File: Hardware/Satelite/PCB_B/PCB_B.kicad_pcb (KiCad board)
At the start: 2 copper layers, 65 parts, among them IC1 MCP1642B-50I_MS, IC2 MCP1642B-50I_MS, J1 Conector_PCB_B-C, J2 Conector_PCB_A-B, U1 MIC5323-3.3YD5_TR, U2 ADP2108AUJ-3.3, U3 INA194, U4 MCP6001-OT, U5 INA194, U6 MCP6001-OT, U7 INA194, U8 BQ24091DGQT, U9 BQ27441DRZR-G1A

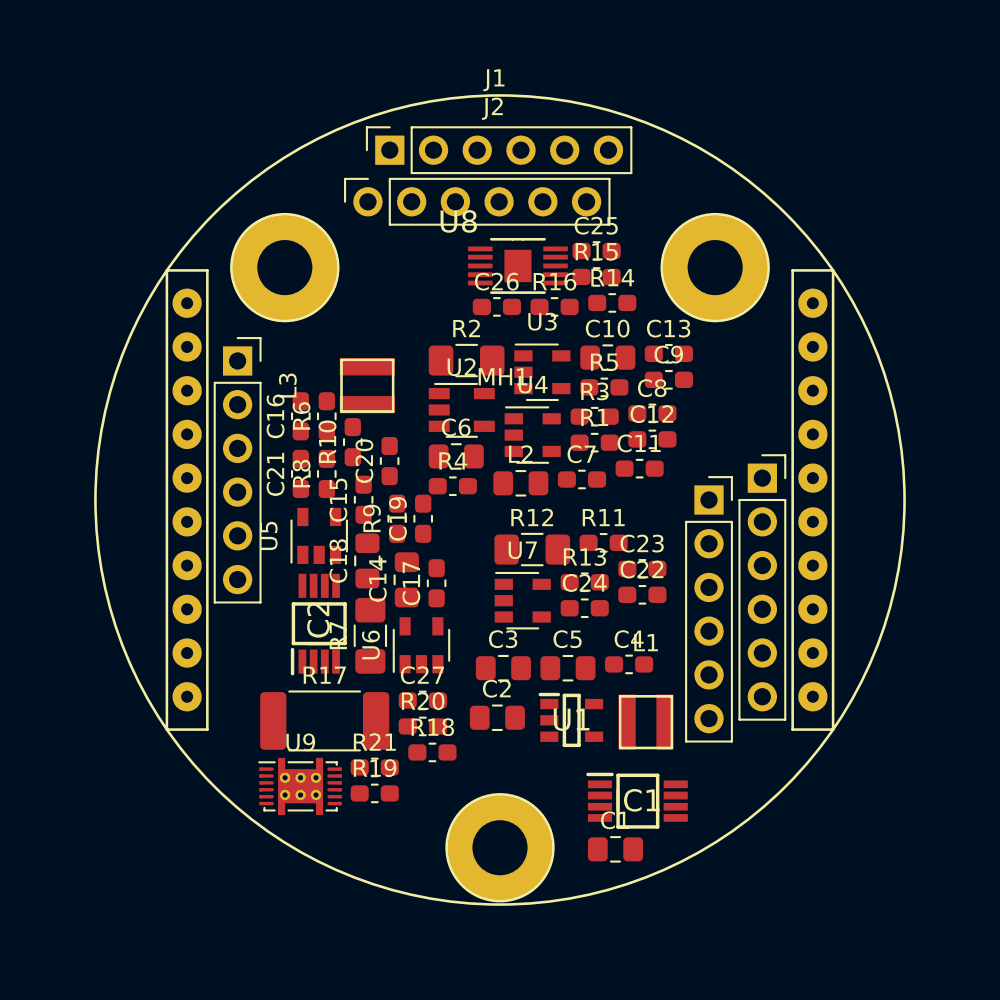
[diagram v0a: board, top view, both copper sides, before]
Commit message: Posicionamiento de conectores en PCB B
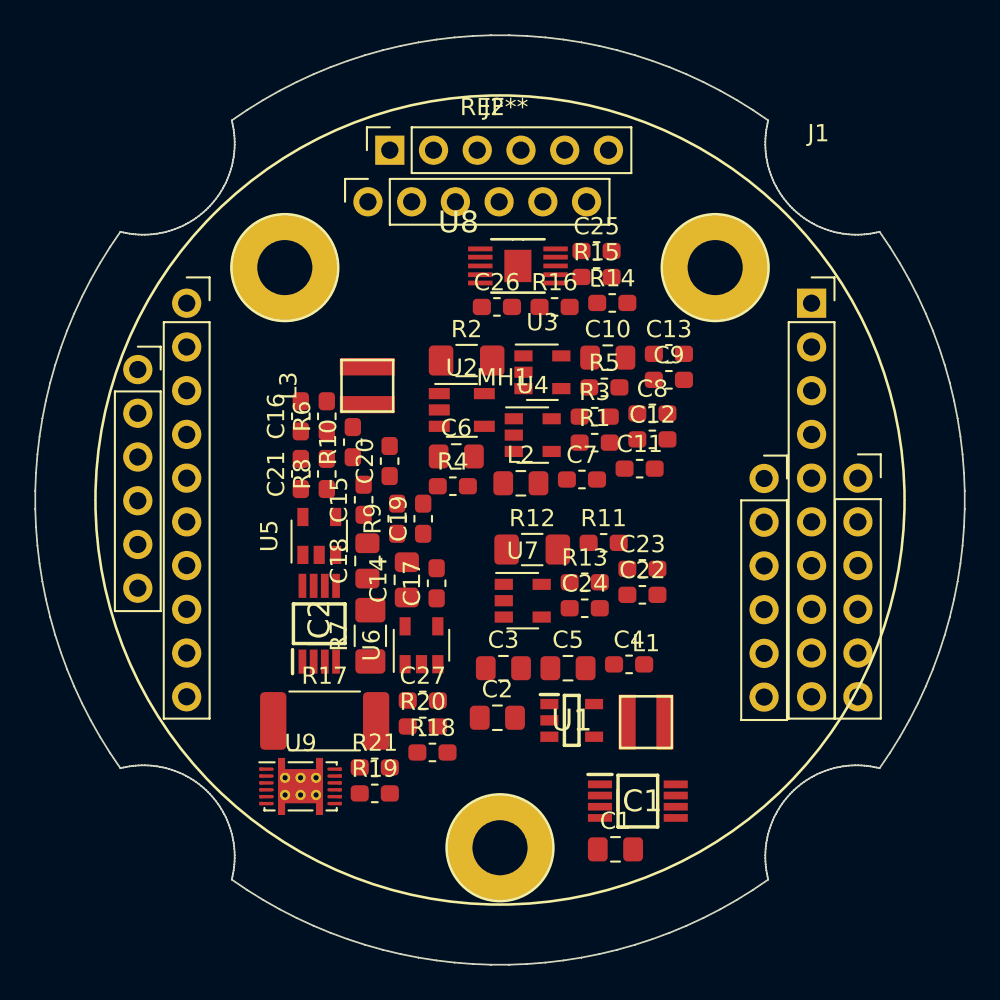
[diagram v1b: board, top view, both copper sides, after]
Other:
- board outline added: 54 x 54 mm

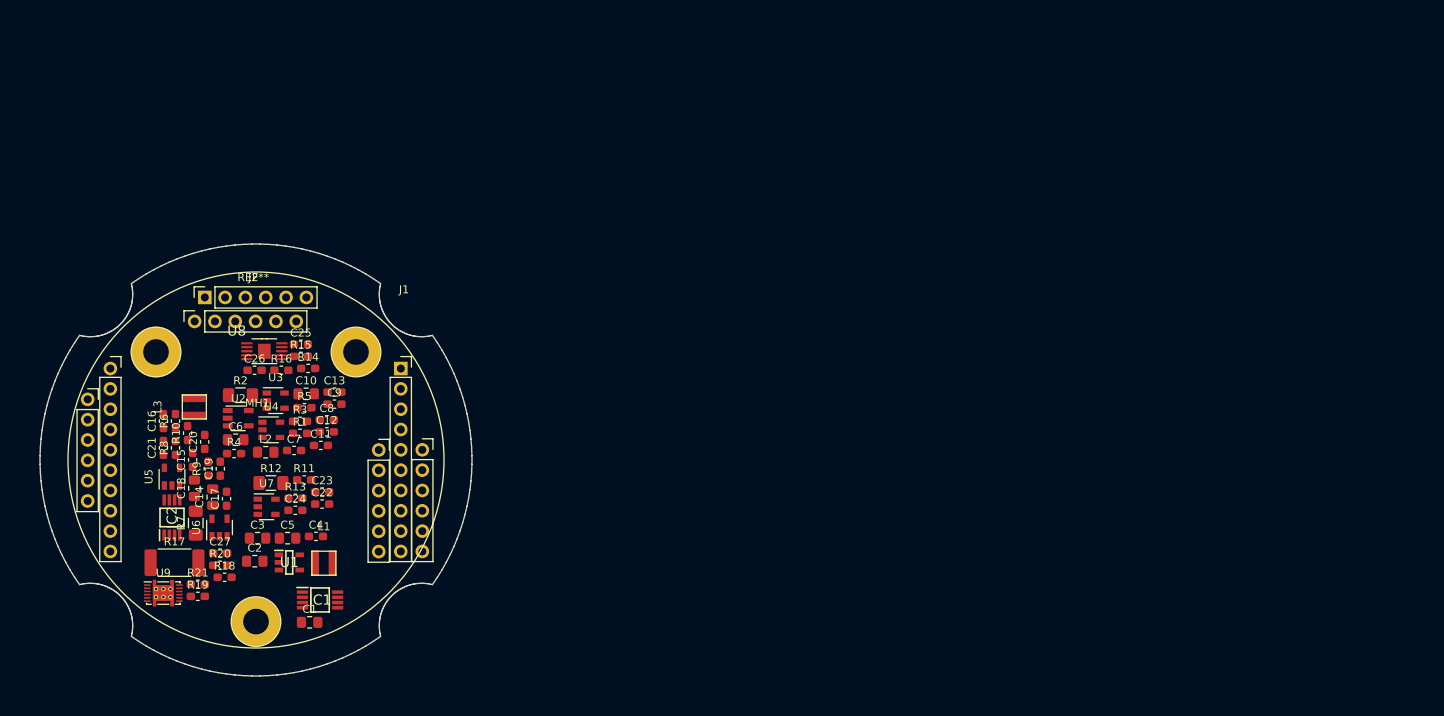
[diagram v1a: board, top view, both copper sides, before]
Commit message: Modificaciones en conectores, netlist para PCB C
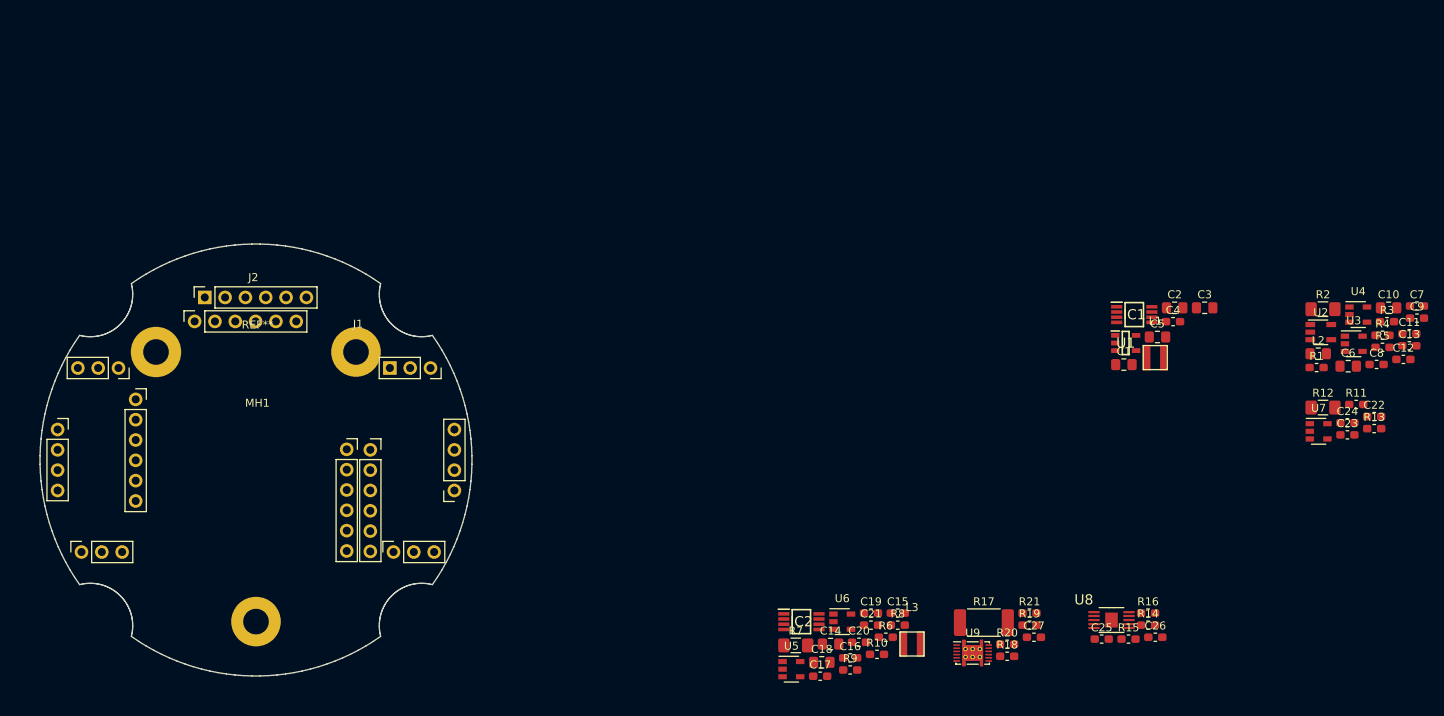
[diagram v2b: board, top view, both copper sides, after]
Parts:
- added REF**: PCB_mayor_diametro, AXTEC:PCB_mayor_diametro, F.Cu at (0.00, 0.00)
- moved R4 144.3 mm to (140.8, -15.6)
- moved C7 141.5 mm to (145.1, -19.2)
- moved C6 139.4 mm to (136.5, -11.7)
- moved C11 136.8 mm to (144.2, -15.8)
- moved U4 136.6 mm to (137.8, -18.2)
- moved R3 136.4 mm to (141.4, -17.3)
- moved C9 135.7 mm to (145.1, -17.7)
- moved R2 135.7 mm to (133.4, -18.9)
- moved U2 135.7 mm to (133.1, -16.0)
- moved C10 135.7 mm to (141.6, -19.0)
- moved R13 135.1 mm to (139.8, -3.92)
- moved R5 135.0 mm to (140.8, -14.1)
- moved U3 134.9 mm to (137.2, -14.5)
- moved C12 134.9 mm to (143.4, -12.6)
- moved C13 134.5 mm to (144.2, -14.3)
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
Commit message: Nuevo conector B-C
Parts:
- IC1, IC2: footprint SOP65P490X110-8N -> SamacSys_Parts:SOP65P490X110-8N
- U1: footprint SOT95P280X100-5N -> SamacSys_Parts:SOT95P280X100-5N

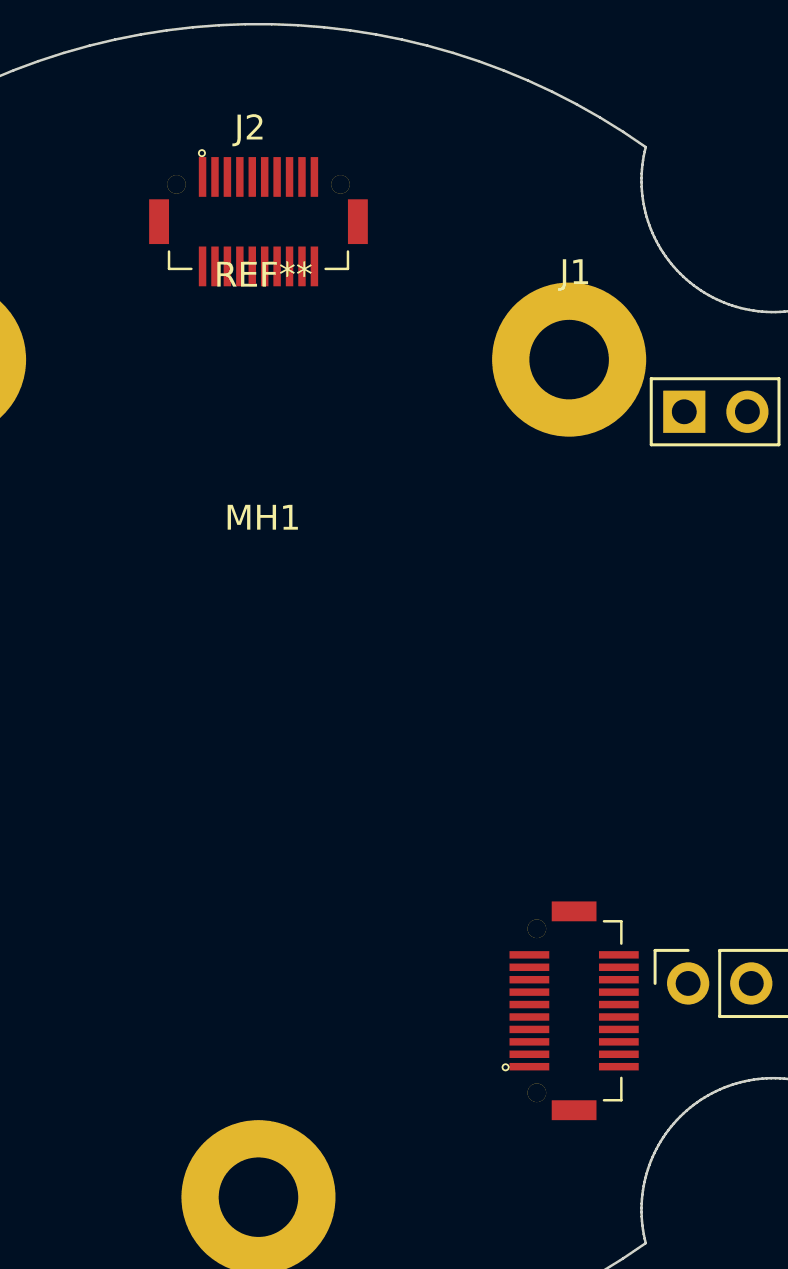
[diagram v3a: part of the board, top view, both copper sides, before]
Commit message: La parte del conector B-C que va en el PCB_B fue movido a bottom mientras que la parte que va en el PCB_C permanece en top
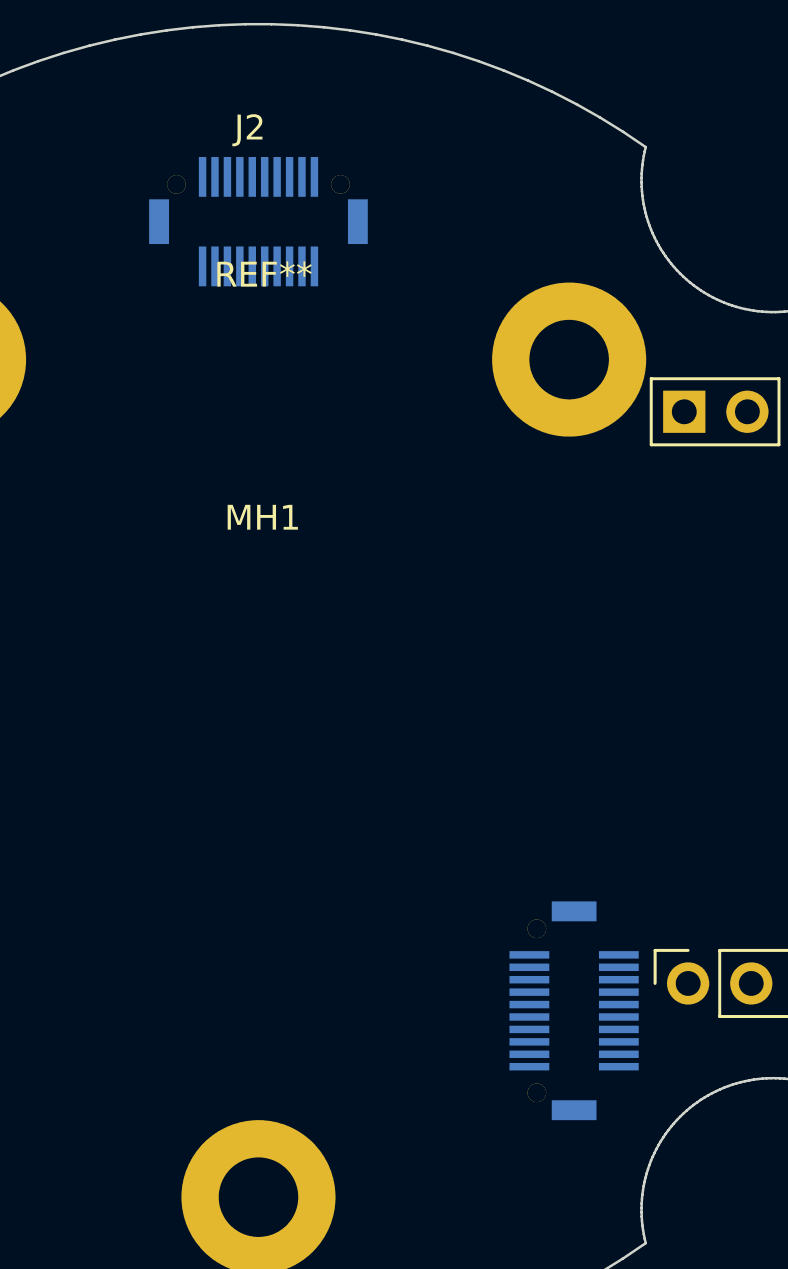
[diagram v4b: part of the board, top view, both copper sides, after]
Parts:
- IC1, IC2: footprint SamacSys_Parts:SOP65P490X110-8N -> SOP65P490X110-8N
- J1: footprint AXTEC:Conector_PCB_B-C -> AXTEC:Conector_PCB_B-C_Lado_B
- U1: footprint SamacSys_Parts:SOT95P280X100-5N -> SOT95P280X100-5N
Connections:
- J1 pad 10: GND -> /I_SENSE_3V3
- J1 pad 11: /V_SENSE_5V -> /V_SENSE_3V3
- J1 pad 12: /V_SENSE_3V3 -> /V_SENSE_5V
- J1 pad 13: /P1 -> GND
- J1 pad 14: /GPS_TX -> +5V
- J1 pad 15: /GPOUT -> GND
- J1 pad 16: /CHG -> GND
- J1 pad 17: +3V3_Internal -> GND
- J1 pad 18: /CHG_DISABLE -> +3V3
- J1 pad 19: /SCLK -> +BATT
- J1 pad 2: +3V3 -> +BATT
- J1 pad 20: /CS -> +BATT
- J1 pad 21: /SDI -> /I_SENSE_BATT
- J1 pad 22: /SDO -> /GPS_TX
- J1 pad 23: /S_PARACAIDAS -> /P1
- J1 pad 24: /S_GLOBO -> /SCLK
- J1 pad 25: +5V -> /CS
- J1 pad 26: /ISET -> /SDI
- J1 pad 28: /SDA -> /S_PARACAIDAS
- J1 pad 29: /SCL -> /S_GLOBO
- J1 pad 3: GND -> +3V3
- J1 pad 30: /I_SENSE_BATT -> /GPOUT
- J1 pad 31: (no net) -> /SDA
- J1 pad 32: (no net) -> /SCL
- J1 pad 33: (no net) -> /CHG_DISABLE
- J1 pad 34: (no net) -> /ISET
- J1 pad 35: (no net) -> /CHG
- J1 pad 36: (no net) -> GND
- J1 pad 37: (no net) -> GND
- J1 pad 38: (no net) -> GND
- J1 pad 39: (no net) -> GND
- J1 pad 40: (no net) -> GND
- J1 pad 41: (no net) -> Net-(J1-Pad41)
- J1 pad 42: (no net) -> Net-(J1-Pad42)
- J1 pad 43: (no net) -> Net-(J1-Pad43)
- J1 pad 44: (no net) -> Net-(J1-Pad44)
- J1 pad 5: /I_SENSE_5V -> GND
- J1 pad 6: /I_SENSE_3V3 -> GND
- J1 pad 7: +BATT -> +5V
- J1 pad 8: +3V3 -> GND
- J1 pad 9: GND -> /I_SENSE_5V

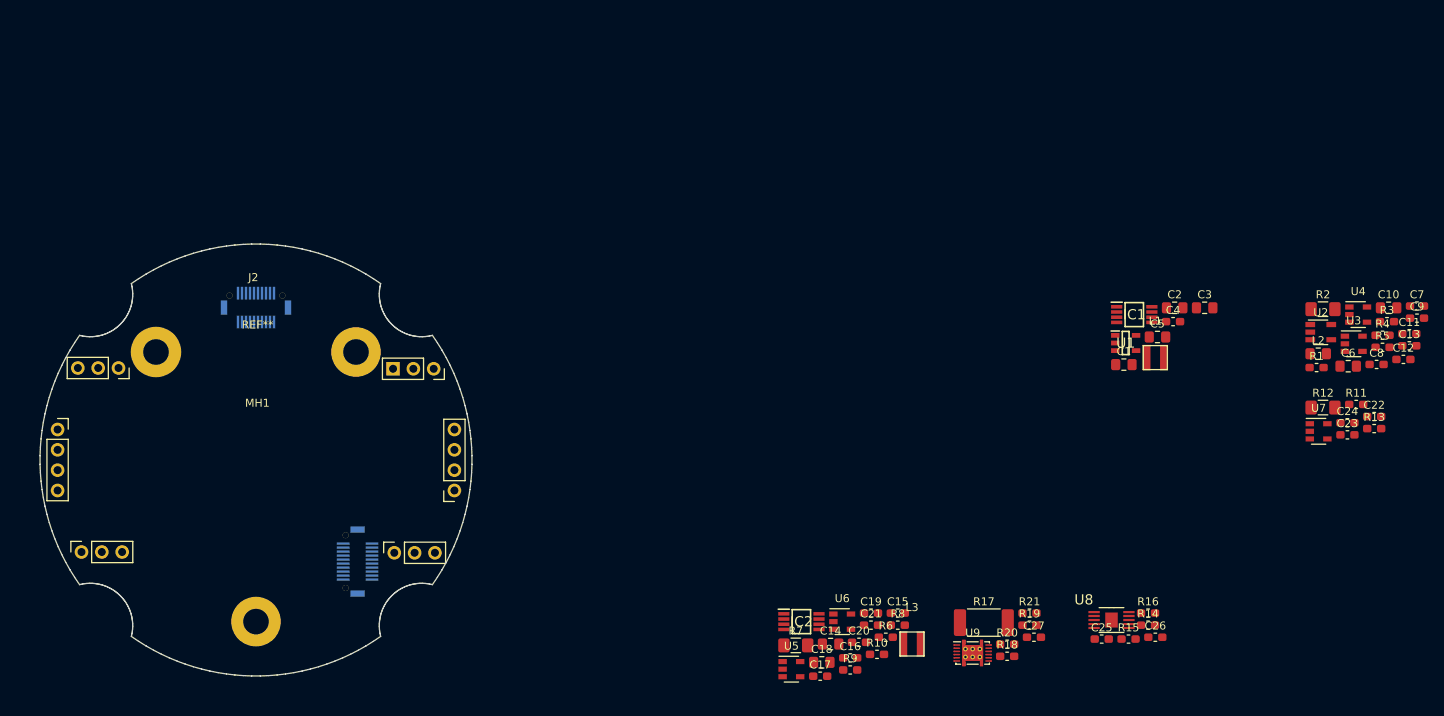
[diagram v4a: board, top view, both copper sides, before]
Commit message: Agregado enable de 3v3 y 5v en PCB B. Diseño WIP
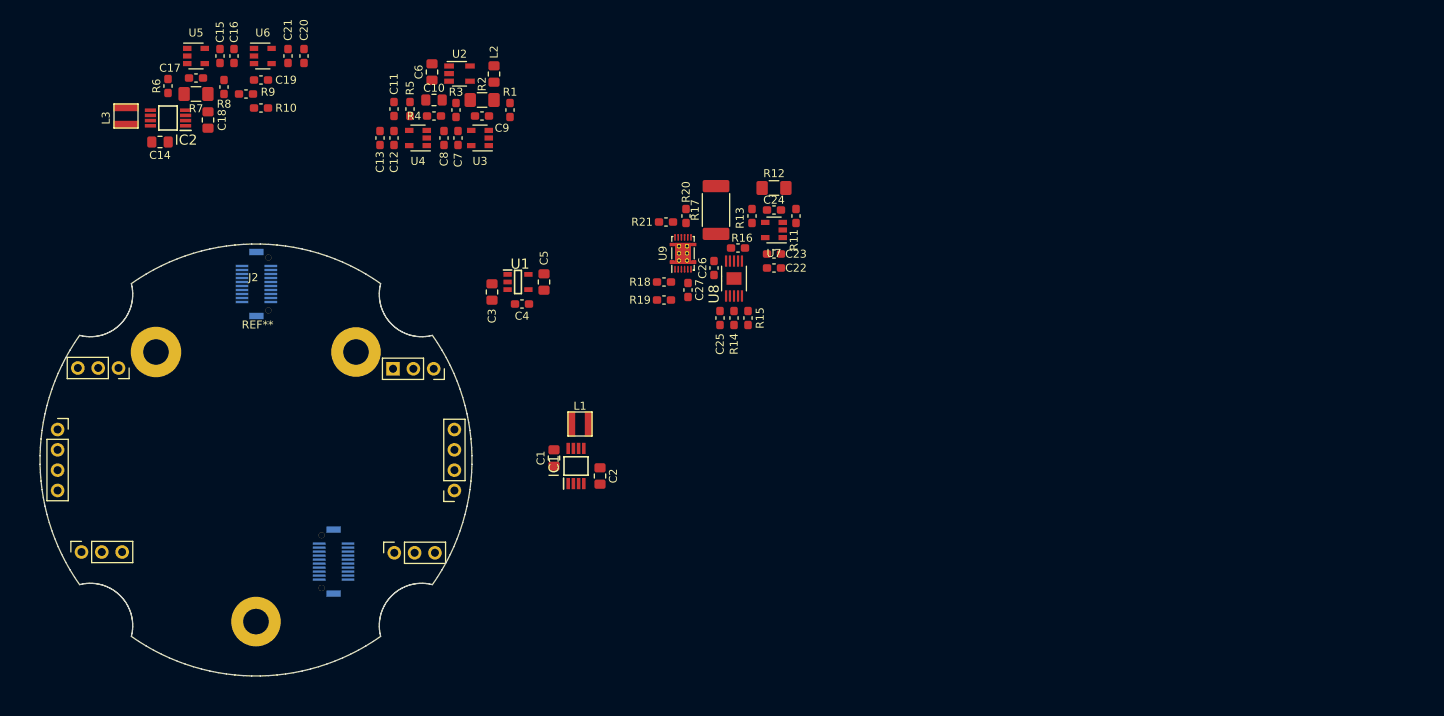
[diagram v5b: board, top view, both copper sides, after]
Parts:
- moved C13 131.3 mm to (15.5, -40.2), turned to 270 degrees
- moved C11 130.0 mm to (17.2, -43.9), turned to 270 degrees
- moved C12 129.2 mm to (17.2, -40.2), turned to 270 degrees
- moved R5 125.2 mm to (19.2, -43.9), turned to 270 degrees
- moved C10 122.1 mm to (22.2, -45.0)
- moved C7 121.7 mm to (25.2, -40.2), turned to 270 degrees
- moved R4 121.7 mm to (22.2, -43.0)
- moved C6 120.3 mm to (22.0, -48.5), turned to 90 degrees
- moved C8 120.0 mm to (23.5, -40.2), turned to 270 degrees
- moved U4 119.6 mm to (20.2, -40.2), turned to 180 degrees
- moved C9 119.6 mm to (28.2, -43.0)
- moved R3 119.3 mm to (25.0, -43.8), turned to 270 degrees
- moved L3 118.4 mm to (-16.2, -43.0), turned to 270 degrees
- moved R6 113.1 mm to (-11.0, -46.8), turned to 90 degrees
- moved U2 112.4 mm to (25.4, -48.3)
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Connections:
- R12 pad 1: /Sensado Corriente/OUT -> /Fuel Gauge/VBAT
- R13 pad 2: /Sensado Corriente/OUT -> /Fuel Gauge/VBAT
